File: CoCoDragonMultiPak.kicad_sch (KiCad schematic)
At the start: 56 parts, among them IC1 74LS245DWR, IC11 74LS153DR, IC2 74LS367ADR, IC3 74LS367ADR, IC4 74LS367ADR, IC5 74LS367ADR, IC6 74LS367ADR, IC7 74LS374DWR, IC8 74LS368AD, IC9 74LS139ADR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

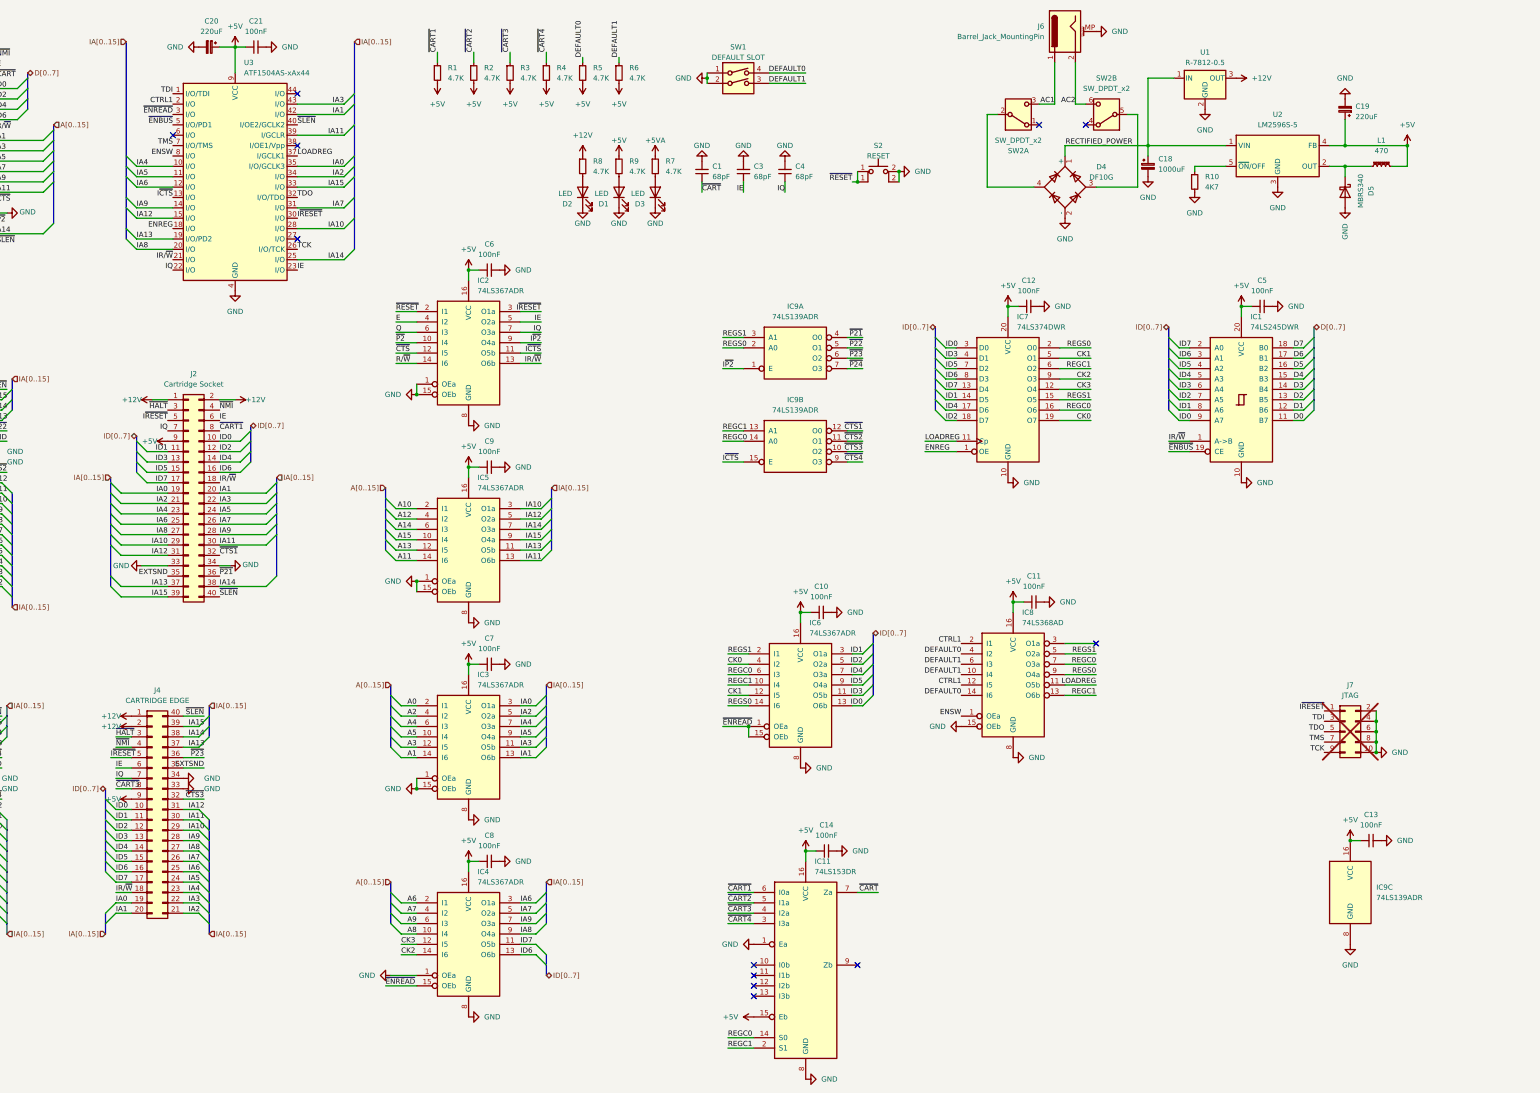
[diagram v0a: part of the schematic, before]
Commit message: convert to ATF1508
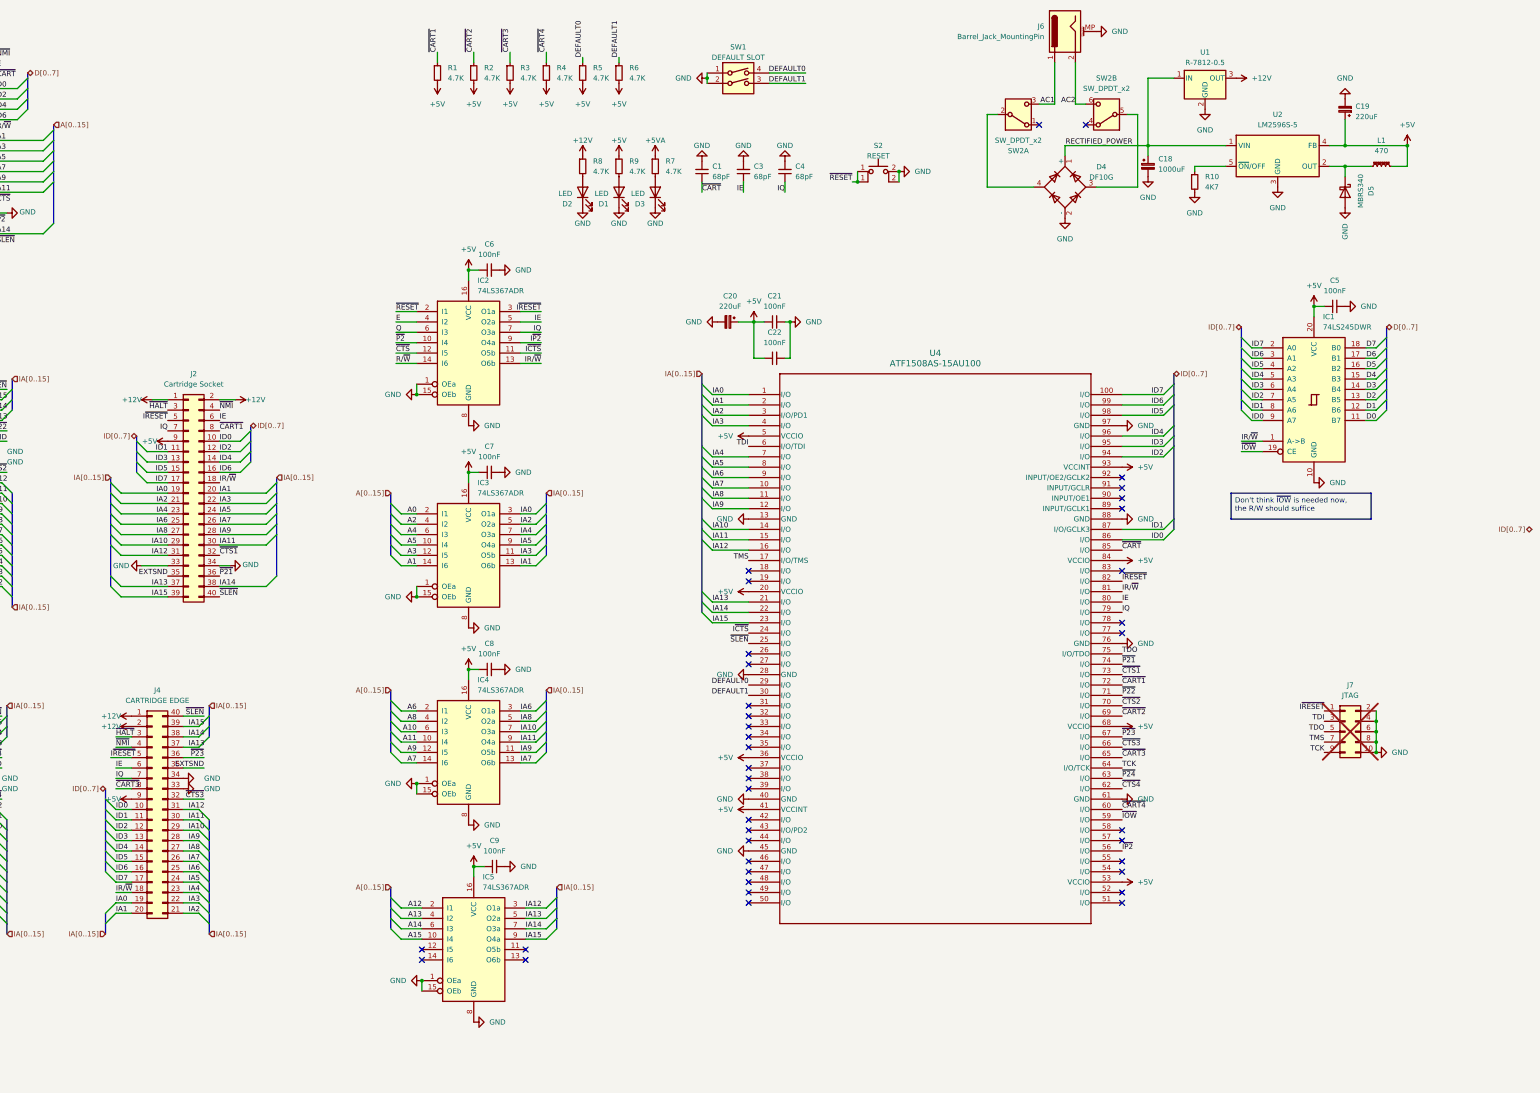
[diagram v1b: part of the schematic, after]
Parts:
- removed C10, C11, C12, C13, C14: 100nF, Capacitor_SMD:C_0805_2012Metric_Pad1.18x1.45mm_HandSolder, symbol Device:C_Small
- removed IC11: 74LS153DR, Package_SO:SOIC-16_3.9x9.9mm_P1.27mm, symbol 74xx:74LS153
- removed IC6: 74LS367ADR, Package_SO:SOIC-16_3.9x9.9mm_P1.27mm, symbol 74xx:74LS367
- removed IC7: 74LS374DWR, Package_SO:SOIC-20W_7.5x12.8mm_P1.27mm, symbol 74xx:74LS374
- removed IC8: 74LS368AD, Package_SO:SOIC-16_3.9x9.9mm_P1.27mm, symbol 74xx:74LS368
- removed IC9: 74LS139ADR, Package_SO:SOIC-16_3.9x9.9mm_P1.27mm, symbol 74xx:74LS139
- removed U3: ATF1504AS-xAx44, Package_QFP:TQFP-44_10x10mm_P0.8mm, symbol CPLD_Microchip:ATF1504AS-xAx44
- added C22: 100nF, Capacitor_SMD:C_0805_2012Metric_Pad1.18x1.45mm_HandSolder, symbol Device:C_Small
- added U4: ATF1508AS-15AU100, Package_QFP:LQFP-100_14x14mm_P0.5mm, symbol Library:ATF1508ASV-15AU100
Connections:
- net CK2 is gone; now on net A7: IC4.14 (I6)
- net CK3 is gone; now on net A9: IC4.12 (I5)
- net ~{ENREAD} is gone; now on net GND: IC4.15 (OEb)
- net +5V: now also C22.1, U4.20 (VCCIO), U4.36 (VCCIO), U4.41 (VCCINT), U4.5 (VCCIO), U4.53 (VCCIO), U4.68 (VCCIO), U4.84 (VCCIO), U4.93 (VCCINT)
- net A10: now also IC4.6 (I3); no longer IC5.2 (I1)
- net A11: now also IC4.10 (I4); no longer IC5.14 (I6)
- net A12: now also IC5.2 (I1); no longer IC5.4 (I2)
- net A13: now also IC5.4 (I2); no longer IC5.12 (I5)
- net A7: no longer IC4.4 (I2)
- net A8: now also IC4.4 (I2); no longer IC4.10 (I4)
- net A9: no longer IC4.6 (I3)
- net DEFAULT0: now also U4.29 (I/O)
- net DEFAULT1: now also U4.30 (I/O)
- net GND: now also C22.2, U4.13 (GND), U4.28 (GND), U4.40 (GND), U4.45 (GND), U4.61 (GND), U4.76 (GND), U4.88 (GND), U4.97 (GND)
- net IA0: now also U4.1 (I/O)
- net IA1: now also U4.2 (I/O)
- net IA10: now also IC4.7 (O3a), U4.14 (I/O); no longer IC5.3 (O1a)
- net IA11: now also IC4.9 (O4a), U4.15 (I/O); no longer IC5.13 (O6b)
- net IA12: now also IC5.3 (O1a), U4.16 (I/O); no longer IC5.5 (O2a)
- net IA13: now also IC5.5 (O2a), U4.21 (I/O); no longer IC5.11 (O5b)
- net IA14: now also U4.22 (I/O)
- net IA15: now also U4.23 (I/O)
- net IA2: now also U4.3 (I/O/PD1)
- net IA3: now also U4.4 (I/O)
- net IA4: now also U4.7 (I/O)
- net IA5: now also U4.8 (I/O)
- net IA6: now also U4.9 (I/O)
- net IA7: now also IC4.13 (O6b), U4.10 (I/O); no longer IC4.5 (O2a)
- net IA8: now also IC4.5 (O2a), U4.11 (I/O); no longer IC4.9 (O4a)
- net IA9: now also IC4.11 (O5b), U4.12 (I/O); no longer IC4.7 (O3a)
- net ID0: now also U4.86 (I/O)
- net ID1: now also U4.87 (I/O/GCLK3)
- net ID2: now also U4.94 (I/O)
- net ID3: now also U4.95 (I/O)
- net ID4: now also U4.96 (I/O)
- net ID5: now also U4.98 (I/O)
- net ID6: now also U4.99 (I/O); no longer IC4.13 (O6b)
- net ID7: now also U4.100 (I/O); no longer IC4.11 (O5b)
- net IE: now also U4.80 (I/O)
- net IQ: now also U4.79 (I/O)
- net IR/~{W}: now also U4.81 (I/O)
- net I~{CTS}: now also U4.24 (I/O)
- net I~{P2}: now also U4.56 (I/O)
- net I~{RESET}: now also U4.82 (I/O)
- net TCK: now also U4.64 (I/O/TCK)
- net TDI: now also U4.6 (I/O/TDI)
- net TDO: now also U4.75 (I/O/TDO)
- net TMS: now also U4.17 (I/O/TMS)
- net ~{CART1}: now also U4.72 (I/O)
- net ~{CART2}: now also U4.69 (I/O)
- net ~{CART3}: now also U4.65 (I/O)
- net ~{CART4}: now also U4.60 (I/O)
- net ~{CART}: now also U4.85 (I/O)
- net ~{CTS1}: now also U4.73 (I/O)
- net ~{CTS2}: now also U4.70 (I/O)
- net ~{CTS3}: now also U4.66 (I/O)
- net ~{CTS4}: now also U4.62 (I/O)
- net ~{P21}: now also U4.74 (I/O)
- net ~{P22}: now also U4.71 (I/O)
- net ~{P23}: now also U4.67 (I/O)
- net ~{P24}: now also U4.63 (I/O)
- net ~{SLEN}: now also U4.25 (I/O)
- net ~{ENBUS} renamed ~{IOW}
- net ~{IOW}: now also U4.59 (I/O)
- no-connect marks 14 -> 41
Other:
- moved on the sheet: C20, C21, C5, C7, C8, C9, IC1, IC3, IC4, IC5
